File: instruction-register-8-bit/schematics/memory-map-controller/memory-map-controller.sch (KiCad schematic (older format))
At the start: 11 parts

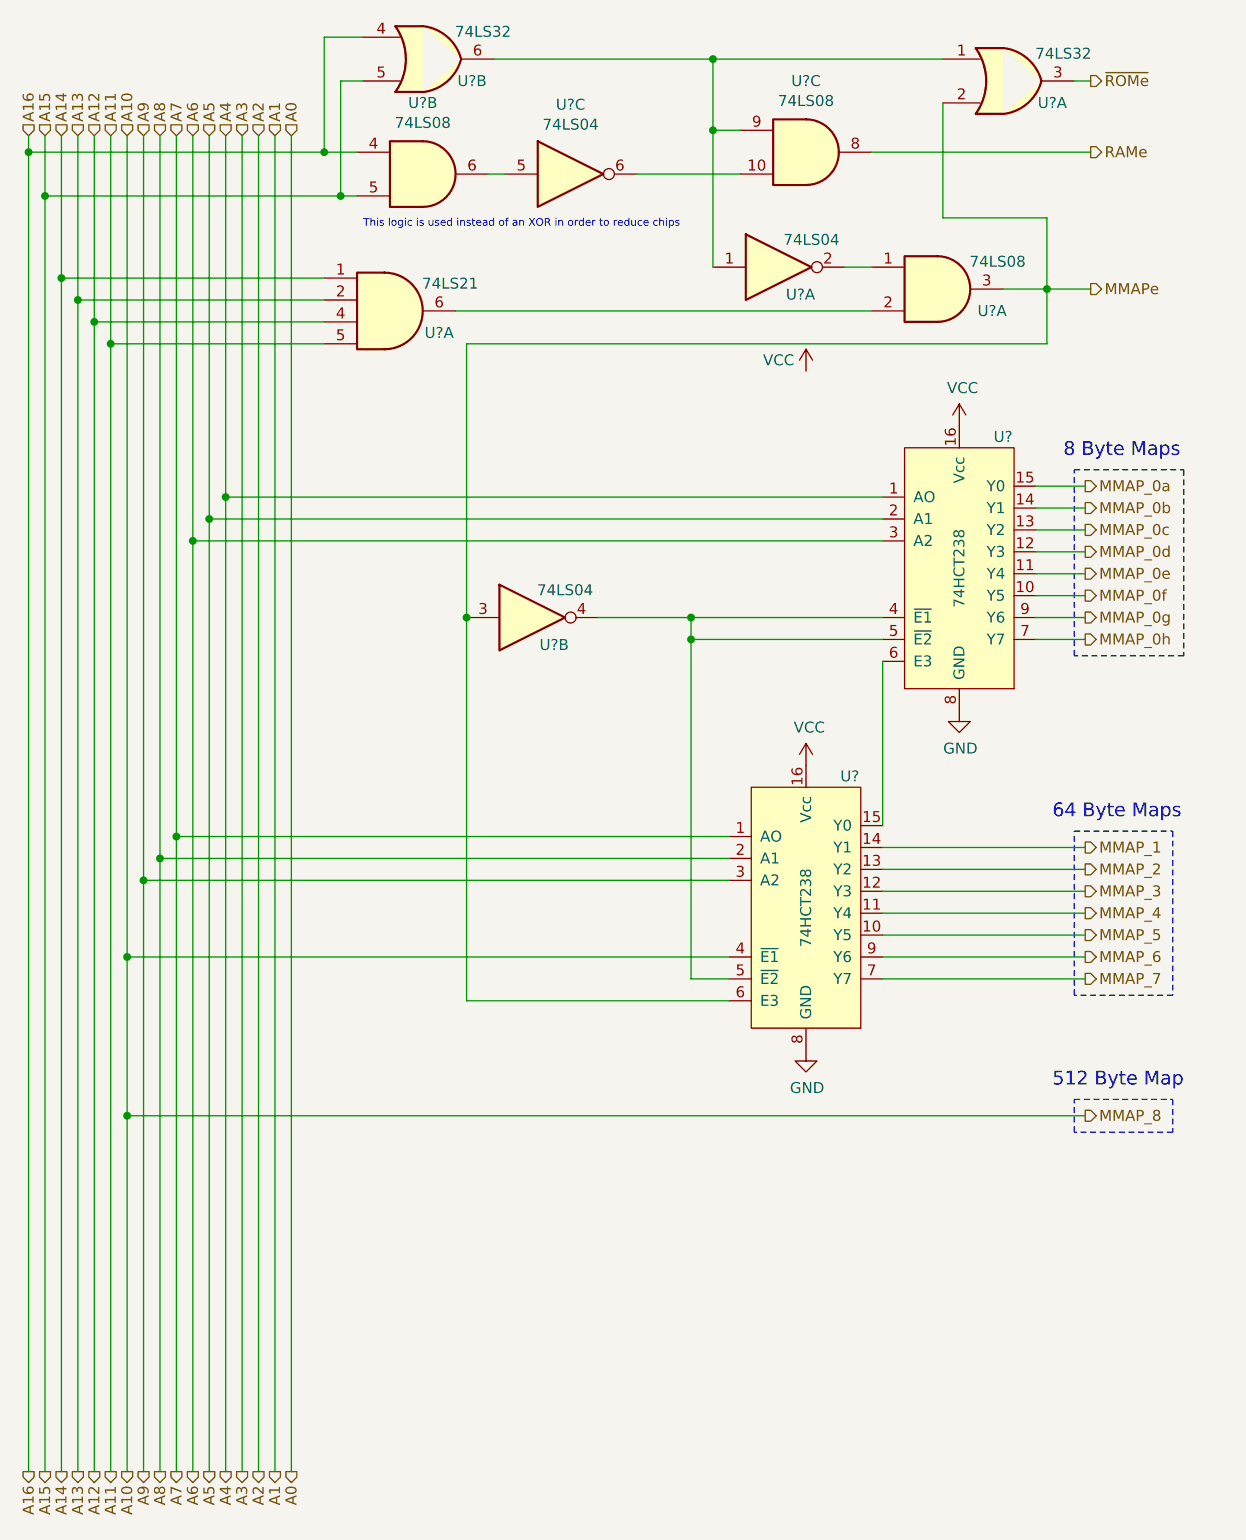
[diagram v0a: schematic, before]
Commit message: removed A16 address line
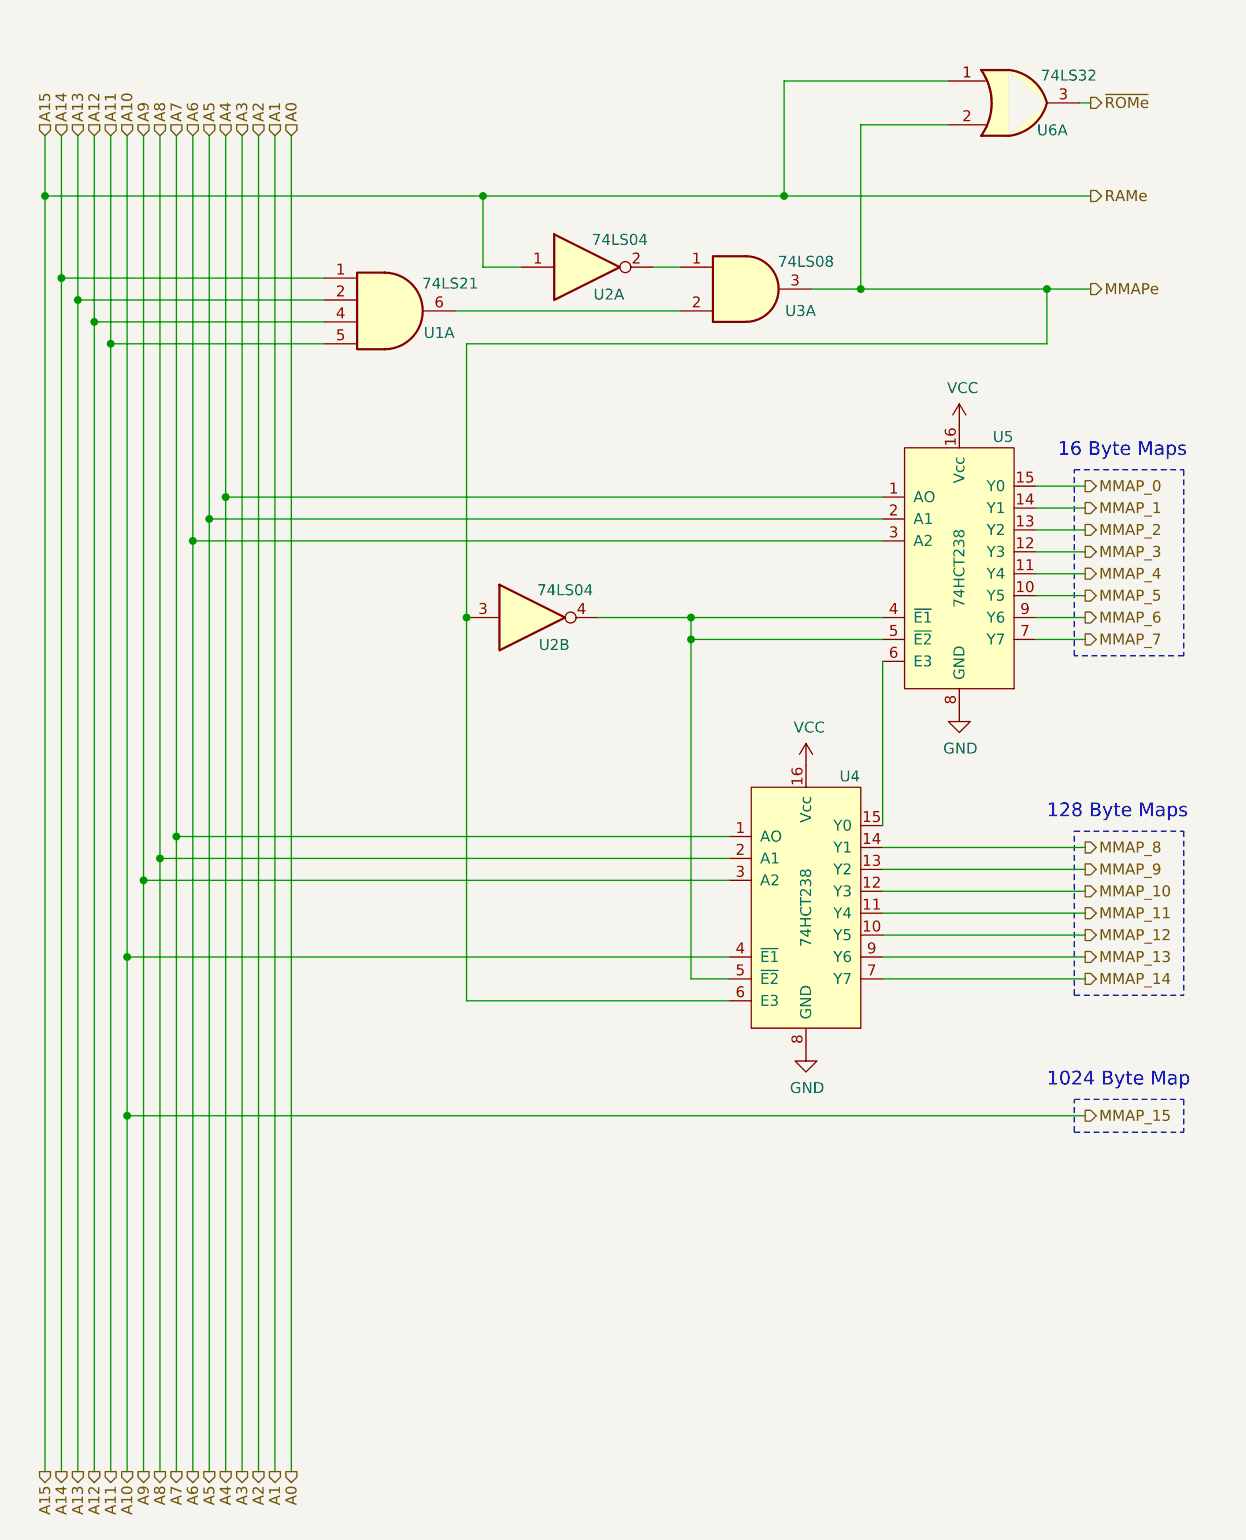
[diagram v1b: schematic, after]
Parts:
- removed U? (x2): 74LS32, symbol 74xx:74LS32
- removed U? (x2): 74LS08, symbol 74xx:74LS08
- removed U?: 74LS04, symbol 74xx:74LS04
- added U6: 74LS32, symbol 74xx:74LS32
- gave numbers to parts that had none: 5
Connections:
- net MMAP_0b is gone; now on net MMAP_1: U5.14 (Y1)
- net MMAP_0c is gone; now on net MMAP_2: U5.13 (Y2)
- net MMAP_0d is gone; now on net MMAP_3: U5.12 (Y3)
- net MMAP_0e is gone; now on net MMAP_4: U5.11 (Y4)
- net MMAP_0f is gone; now on net MMAP_5: U5.10 (Y5)
- net MMAP_0g is gone; now on net MMAP_6: U5.9 (Y6)
- net MMAP_0h is gone; now on net MMAP_7: U5.7 (Y7)
- net A15: now also U2.1, U6.1
- net MMAP_1: no longer U4.14 (Y1)
- net MMAP_2: no longer U4.13 (Y2)
- net MMAP_3: no longer U4.12 (Y3)
- net MMAP_4: no longer U4.11 (Y4)
- net MMAP_5: no longer U4.10 (Y5)
- net MMAP_6: no longer U4.9 (Y6)
- net MMAP_7: no longer U4.7 (Y7)
- net MMAPe: now also U6.2
- net ~ROMe: now also U6.3
- net MMAP_0a renamed MMAP_0
- new net MMAP_10: U4.12 (Y3)
- new net MMAP_11: U4.11 (Y4)
- new net MMAP_12: U4.10 (Y5)
- new net MMAP_13: U4.9 (Y6)
- new net MMAP_14: U4.7 (Y7)
- new net MMAP_8: U4.14 (Y1)
- new net MMAP_9: U4.13 (Y2)
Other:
- note added: "1024 Byte Map"
- note added: "128 Byte Maps"
- note added: "16 Byte Maps"
- note removed: "512 Byte Map"
- note removed: "64 Byte Maps"
- note removed: "8 Byte Maps"
- note removed: "This logic is used instead of an XOR in order to reduce chips"
- moved on the sheet: U2A, U3A
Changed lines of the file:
@@
 Wire Wire Line
 	1550 7150 1550 1700
-Text HLabel 6250 1125 2    50   Output ~ 0
+Text HLabel 6250 1325 2    50   Output ~ 0
 RAMe
 $Comp
-L 74xx:74LS21 U?
+L 74xx:74LS21 U1
 U 1 1 610A2B3A
 P 3050 1850
-F 0 "U?" H 3275 1750 50  0000 C CNN
+F 0 "U1" H 3275 1750 50  0000 C CNN
 F 1 "74LS21" H 3325 1975 50  0000 C CNN
 F 2 "" H 3050 1850 50  0001 C CNN
@@
 $EndComp
 $Comp
-L 74xx:74LS04 U?
+L 74xx:74LS04 U2
 U 1 1 610A4EC8
-P 4825 1650
-F 0 "U?" H 4925 1525 50  0000 C CNN
-F 1 "74LS04" H 4975 1775 50  0000 C CNN
-F 2 "" H 4825 1650 50  0001 C CNN
-F 3 "http://www.ti.com/lit/gpn/sn74LS04" H 4825 1650 50  0001 C CNN
-	1    4825 1650
+P 3950 1650
+F 0 "U2" H 4050 1525 50  0000 C CNN
+F 1 "74LS04" H 4100 1775 50  0000 C CNN
+F 2 "" H 3950 1650 50  0001 C CNN
+F 3 "http://www.ti.com/lit/gpn/sn74LS04" H 3950 1650 50  0001 C CNN
+	1    3950 1650
 	1    0    0    -1
 $EndComp
@@
 Text HLabel 6250 1750 2    50   Output ~ 0
 MMAPe
-Text HLabel 6250 800  2    50   Output ~ 0
+Text HLabel 6250 900  2    50   Output ~ 0
 ~ROMe
-Wire Wire Line
-	6175 800  6250 800
-$Comp
-L common-symbols:74HCT238 U?
+$Comp
+L common-symbols:74HCT238 U5
 U 1 1 610C0683
 P 5650 3000
-F 0 "U?" H 5850 3575 50  0000 C CNN
+F 0 "U5" H 5850 3575 50  0000 C CNN
 F 1 "74HCT238" V 5650 2975 50  0000 C CNN
 F 2 "" H 5500 2825 50  0001 C CNN
@@
 $EndComp
 $Comp
-L common-symbols:74HCT238 U?
+L common-symbols:74HCT238 U4
 U 1 1 610C819E
 P 4950 4550
-F 0 "U?" H 5150 5125 50  0000 C CNN
+F 0 "U4" H 5150 5125 50  0000 C CNN
 F 1 "74HCT238" V 4950 4525 50  0000 C CNN
 F 2 "" H 4800 4375 50  0001 C CNN
@@
 	2300 2700 2300 7150
 $Comp
-L 74xx:74LS04 U?
+L 74xx:74LS04 U2
 U 2 1 610D71D6
 P 3700 3250
-F 0 "U?" H 3800 3125 50  0000 C CNN
+F 0 "U2" H 3800 3125 50  0000 C CNN
 F 1 "74LS04" H 3850 3375 50  0000 C CNN
 F 2 "" H 3700 3250 50  0001 C CNN
@@
 Connection ~ 3400 3250
 Text HLabel 6225 2650 2    50   Output ~ 0
-MMAP_0a
+MMAP_0
 Text HLabel 6225 2750 2    50   Output ~ 0
-MMAP_0b
+MMAP_1
 Text HLabel 6225 2850 2    50   Output ~ 0
-MMAP_0c
+MMAP_2
 Text HLabel 6225 2950 2    50   Output ~ 0
-MMAP_0d
+MMAP_3
 Text HLabel 6225 3050 2    50   Output ~ 0
-MMAP_0e
+MMAP_4
 Text HLabel 6225 3150 2    50   Output ~ 0
-MMAP_0f
+MMAP_5
 Text HLabel 6225 3250 2    50   Output ~ 0
-MMAP_0g
+MMAP_6
 Text HLabel 6225 3350 2    50   Output ~ 0
-MMAP_0h
+MMAP_7
 Wire Wire Line
 	6000 2650 6225 2650
@@
 	6000 3350 6225 3350
 Text HLabel 6225 4300 2    50   Output ~ 0
-MMAP_1
+MMAP_8
 Wire Wire Line
 	5300 4300 6225 4300
 Text HLabel 6225 4400 2    50   Output ~ 0
-MMAP_2
+MMAP_9
 Text HLabel 6225 4500 2    50   Output ~ 0
-MMAP_3
+MMAP_10
 Text HLabel 6225 4600 2    50   Output ~ 0
-MMAP_4
+MMAP_11
 Text HLabel 6225 4700 2    50   Output ~ 0
-MMAP_5
+MMAP_12
 Text HLabel 6225 4800 2    50   Output ~ 0
-MMAP_6
+MMAP_13
 Text HLabel 6225 4900 2    50   Output ~ 0
-MMAP_7
+MMAP_14
 Wire Wire Line
 	5300 4400 6225 4400
@@
 Wire Wire Line
 	6225 4900 5300 4900
-$Comp
-L 74xx:74LS32 U?
-U 1 1 6113D1DF
-P 5875 800
-F 0 "U?" H 6075 700 50  0000 C CNN
-F 1 "74LS32" H 6125 925 50  0000 C CNN
-F 2 "" H 5875 800 50  0001 C CNN
-F 3 "http://www.ti.com/lit/gpn/sn74LS32" H 5875 800 50  0001 C CNN
-	1    5875 800
-	1    0    0    -1
-$EndComp
-Text HLabel 1400 1050 1    50   Input ~ 0
-A16
-Text HLabel 1400 7150 3    50   Output ~ 0
-A16
-Wire Wire Line
-	1400 7150 1400 1125
 Wire Wire Line
 	1475 1050 1475 1325
-Wire Wire Line
-	2900 1125 2750 1125
-Connection ~ 1400 1125
-Wire Wire Line
-	1400 1125 1400 1050
-Wire Wire Line
-	2900 1325 2825 1325
 Connection ~ 1475 1325
 Wire Wire Line
 	1475 1325 1475 7150
 $Comp
-L 74xx:74LS32 U?
-U 2 1 61221DD6
-P 3225 700
-F 0 "U?" H 3425 600 50  0000 C CNN
-F 1 "74LS32" H 3475 825 50  0000 C CNN
-F 2 "" H 3225 700 50  0001 C CNN
-F 3 "http://www.ti.com/lit/gpn/sn74LS32" H 3225 700 50  0001 C CNN
-	2    3225 700
-	1    0    0    -1
-$EndComp
-Wire Wire Line
-	3525 700  4525 700
-Wire Wire Line
-	2825 1325 2825 800
-Wire Wire Line
-	2825 800  2925 800
-Connection ~ 2825 1325
-Wire Wire Line
-	2825 1325 1475 1325
-Wire Wire Line
-	2925 600  2750 600
-Wire Wire Line
-	2750 600  2750 1125
-Connection ~ 2750 1125
-Wire Wire Line
-	2750 1125 1400 1125
-$Comp
-L 74xx:74LS08 U?
+L 74xx:74LS08 U3
 U 1 1 6124CEFE
-P 5550 1750
-F 0 "U?" H 5800 1650 50  0000 C CNN
-F 1 "74LS08" H 5825 1875 50  0000 C CNN
-F 2 "" H 5550 1750 50  0001 C CNN
-F 3 "http://www.ti.com/lit/gpn/sn74LS08" H 5550 1750 50  0001 C CNN
-	1    5550 1750
-	1    0    0    -1
-$EndComp
-Wire Wire Line
-	3350 1850 5250 1850
-Wire Wire Line
-	5125 1650 5250 1650
-Wire Wire Line
-	4525 1650 4525 1025
-Connection ~ 4525 700
-Wire Wire Line
-	4525 700  5575 700
-Wire Wire Line
-	5850 1750 6050 1750
-Wire Wire Line
-	6050 1750 6050 1425
-Wire Wire Line
-	6050 1425 5575 1425
-Wire Wire Line
-	5575 1425 5575 900
+P 4675 1750
+F 0 "U3" H 4925 1650 50  0000 C CNN
+F 1 "74LS08" H 4950 1875 50  0000 C CNN
+F 2 "" H 4675 1750 50  0001 C CNN
+F 3 "http://www.ti.com/lit/gpn/sn74LS08" H 4675 1750 50  0001 C CNN
+	1    4675 1750
+	1    0    0    -1
+$EndComp
+Wire Wire Line
+	3350 1850 4375 1850
+Wire Wire Line
+	4250 1650 4375 1650
+Wire Wire Line
+	4975 1750 5200 1750
 Connection ~ 6050 1750
 Wire Wire Line
@@
 	3400 2000 6050 2000
 $Comp
-L 74xx:74LS08 U?
-U 2 1 61272C32
-P 3200 1225
-F 0 "U?" H 3200 1550 50  0000 C CNN
-F 1 "74LS08" H 3200 1459 50  0000 C CNN
-F 2 "" H 3200 1225 50  0001 C CNN
-F 3 "http://www.ti.com/lit/gpn/sn74LS08" H 3200 1225 50  0001 C CNN
-	2    3200 1225
-	1    0    0    -1
-$EndComp
-$Comp
-L 74xx:74LS04 U?
-U 3 1 61274478
-P 3875 1225
-F 0 "U?" H 3875 1542 50  0000 C CNN
-F 1 "74LS04" H 3875 1451 50  0000 C CNN
-F 2 "" H 3875 1225 50  0001 C CNN
-F 3 "http://www.ti.com/lit/gpn/sn74LS04" H 3875 1225 50  0001 C CNN
-	3    3875 1225
-	1    0    0    -1
-$EndComp
-Wire Wire Line
-	3500 1225 3575 1225
-$Comp
-L 74xx:74LS08 U?
-U 3 1 61279070
-P 4950 1125
-F 0 "U?" H 4950 1450 50  0000 C CNN
-F 1 "74LS08" H 4950 1359 50  0000 C CNN
-F 2 "" H 4950 1125 50  0001 C CNN
-F 3 "http://www.ti.com/lit/gpn/sn74LS08" H 4950 1125 50  0001 C CNN
-	3    4950 1125
-	1    0    0    -1
-$EndComp
-Wire Wire Line
-	4175 1225 4650 1225
-Wire Wire Line
-	4650 1025 4525 1025
-Connection ~ 4525 1025
-Wire Wire Line
-	4525 1025 4525 700
-Wire Wire Line
-	5250 1125 6250 1125
-Text Notes 4375 1475 2    35   ~ 0
-This logic is used instead of an XOR in order to reduce chips
-$Comp
-L power:VCC #PWR?
+L power:VCC #PWR0101
 U 1 1 61442B67
 P 5650 2375
-F 0 "#PWR?" H 5650 2225 50  0001 C CNN
+F 0 "#PWR0101" H 5650 2225 50  0001 C CNN
 F 1 "VCC" H 5665 2548 50  0000 C CNN
 F 2 "" H 5650 2375 50  0001 C CNN
@@
 $EndComp
 $Comp
-L power:VCC #PWR?
+L power:VCC #PWR0102
 U 1 1 61443128
 P 4950 3925
-F 0 "#PWR?" H 4950 3775 50  0001 C CNN
+F 0 "#PWR0102" H 4950 3775 50  0001 C CNN
 F 1 "VCC" H 4965 4098 50  0000 C CNN
 F 2 "" H 4950 3925 50  0001 C CNN
@@
 $EndComp
 $Comp
-L power:VCC #PWR?
-U 1 1 61443D3F
-P 4950 2125
-F 0 "#PWR?" H 4950 1975 50  0001 C CNN
-F 1 "VCC" H 4825 2175 50  0000 C CNN
-F 2 "" H 4950 2125 50  0001 C CNN
-F 3 "" H 4950 2125 50  0001 C CNN
-	1    4950 2125
-	1    0    0    -1
-$EndComp
-$Comp
-L power:GND #PWR?
+L power:GND #PWR0103
 U 1 1 614450AA
 P 5650 3675
-F 0 "#PWR?" H 5650 3425 50  0001 C CNN
+F 0 "#PWR0103" H 5650 3425 50  0001 C CNN
 F 1 "GND" H 5655 3502 50  0000 C CNN
 F 2 "" H 5650 3675 50  0001 C CNN
@@
 $EndComp
 $Comp
-L power:GND #PWR?
+L power:GND #PWR0104
 U 1 1 6144568F
 P 4950 5225
-F 0 "#PWR?" H 4950 4975 50  0001 C CNN
+F 0 "#PWR0104" H 4950 4975 50  0001 C CNN
 F 1 "GND" H 4955 5052 50  0000 C CNN
 F 2 "" H 4950 5225 50  0001 C CNN
@@
 	1850 5525 1850 7150
 Text HLabel 6225 5525 2    50   Output ~ 0
-MMAP_8
+MMAP_15
 Wire Notes Line
 	6175 2575 6675 2575
@@
 Wire Notes Line
 	6175 3425 6175 2575
-Text Notes 6125 2525 0    63   ~ 0
-8 Byte Maps
-Wire Notes Line
-	6175 4225 6625 4225
-Wire Notes Line
-	6625 4225 6625 4975
-Wire Notes Line
-	6625 4975 6175 4975
+Text Notes 6100 2525 0    63   ~ 0
+16 Byte Maps
+Wire Notes Line
+	6675 4225 6675 4975
 Wire Notes Line
 	6175 4975 6175 4225
-Text Notes 6075 4175 0    63   ~ 0
-64 Byte Maps
-Wire Notes Line
-	6175 5450 6625 5450
-Wire Notes Line
-	6625 5450 6625 5600
-Wire Notes Line
-	6625 5600 6175 5600
+Text Notes 6050 4175 0    63   ~ 0
+128 Byte Maps
+Wire Notes Line
+	6675 5450 6675 5600
 Wire Notes Line
 	6175 5600 6175 5450
-Text Notes 6075 5400 0    63   ~ 0
-512 Byte Map
+Text Notes 6050 5400 0    63   ~ 0
+1024 Byte Map
+Wire Wire Line
+	1475 1325 3475 1325
+Wire Wire Line
+	3650 1650 3475 1650
+Wire Wire Line
+	3475 1650 3475 1325
+Connection ~ 3475 1325
+Wire Wire Line
+	3475 1325 4850 1325
+$Comp
+L 74xx:74LS32 U6
+U 1 1 60ED1285
+P 5900 900
+F 0 "U6" H 6075 775 50  0000 C CNN
+F 1 "74LS32" H 6150 1025 50  0000 C CNN
+F 2 "" H 5900 900 50  0001 C CNN
+F 3 "http://www.ti.com/lit/gpn/sn74LS32" H 5900 900 50  0001 C CNN
+	1    5900 900
+	1    0    0    -1
+$EndComp
+Wire Wire Line
+	4850 1325 4850 800
+Wire Wire Line
+	4850 800  5600 800
+Connection ~ 4850 1325
+Wire Wire Line
+	4850 1325 6250 1325
+Wire Wire Line
+	5200 1750 5200 1000
+Wire Wire Line
+	5200 1000 5600 1000
+Connection ~ 5200 1750
+Wire Wire Line
+	5200 1750 6050 1750
+Wire Wire Line
+	6200 900  6250 900
+Wire Notes Line
+	6175 4225 6675 4225
+Wire Notes Line
+	6175 4975 6675 4975
+Wire Notes Line
+	6175 5450 6675 5450
+Wire Notes Line
+	6175 5600 6675 5600
 $EndSCHEMATC
